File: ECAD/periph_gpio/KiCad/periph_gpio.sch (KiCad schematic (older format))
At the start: 0 parts

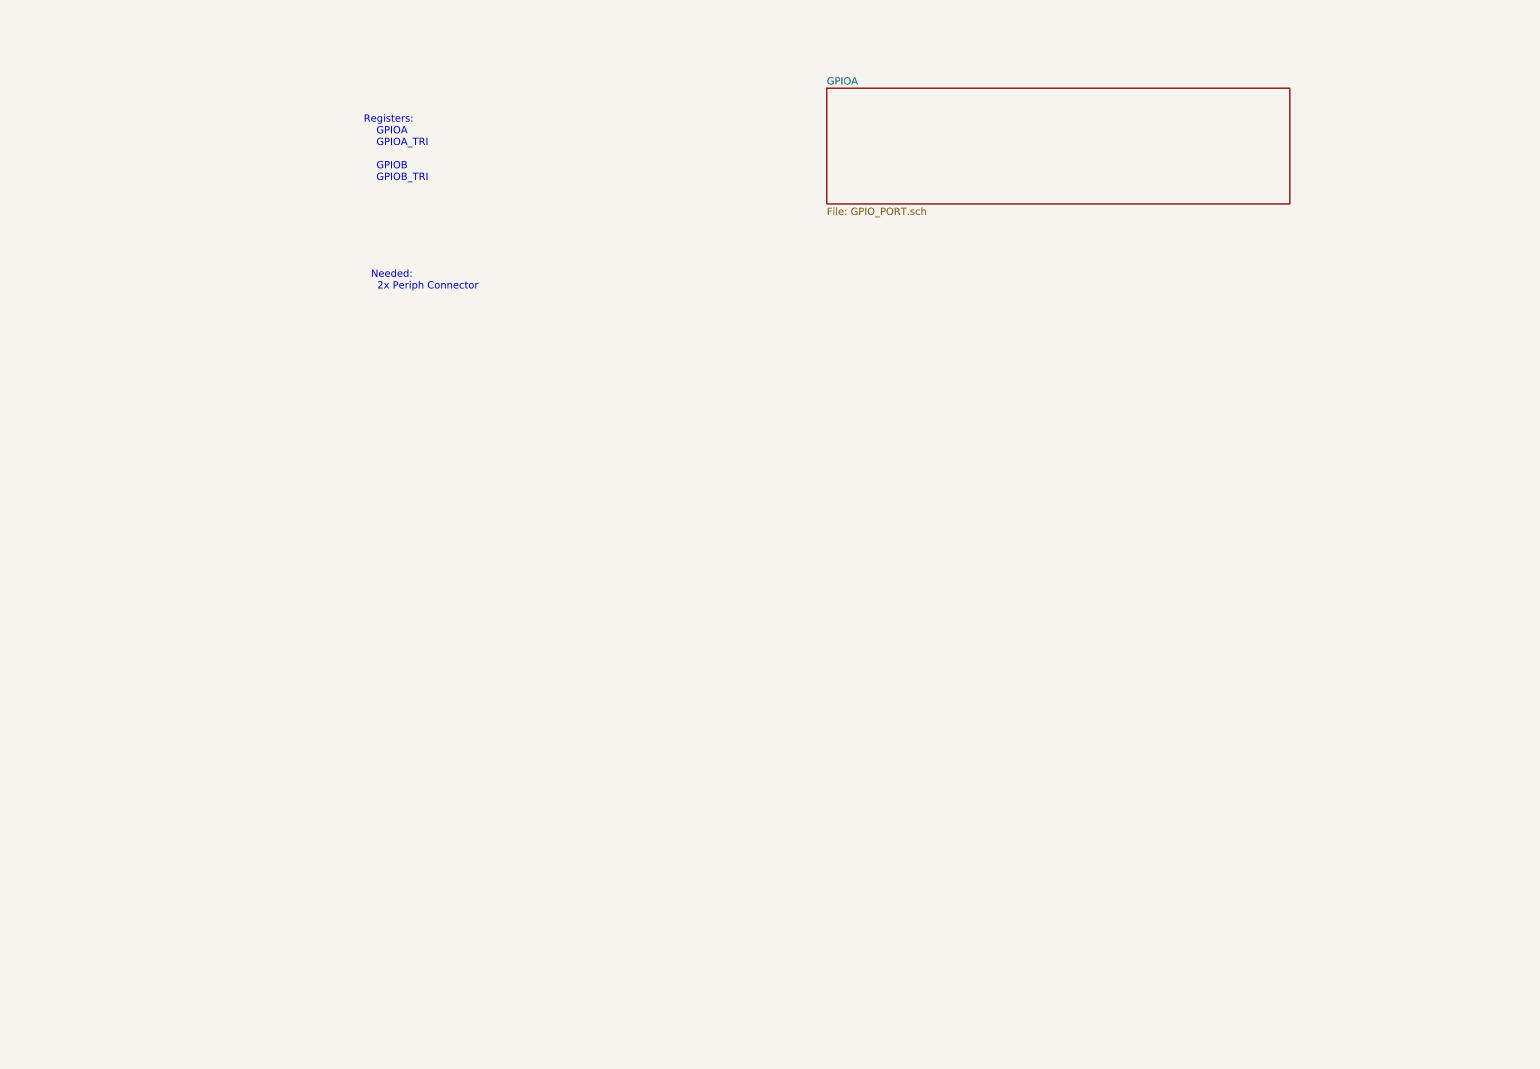
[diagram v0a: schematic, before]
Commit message: First draft v1.0 schematic done, ready for verify
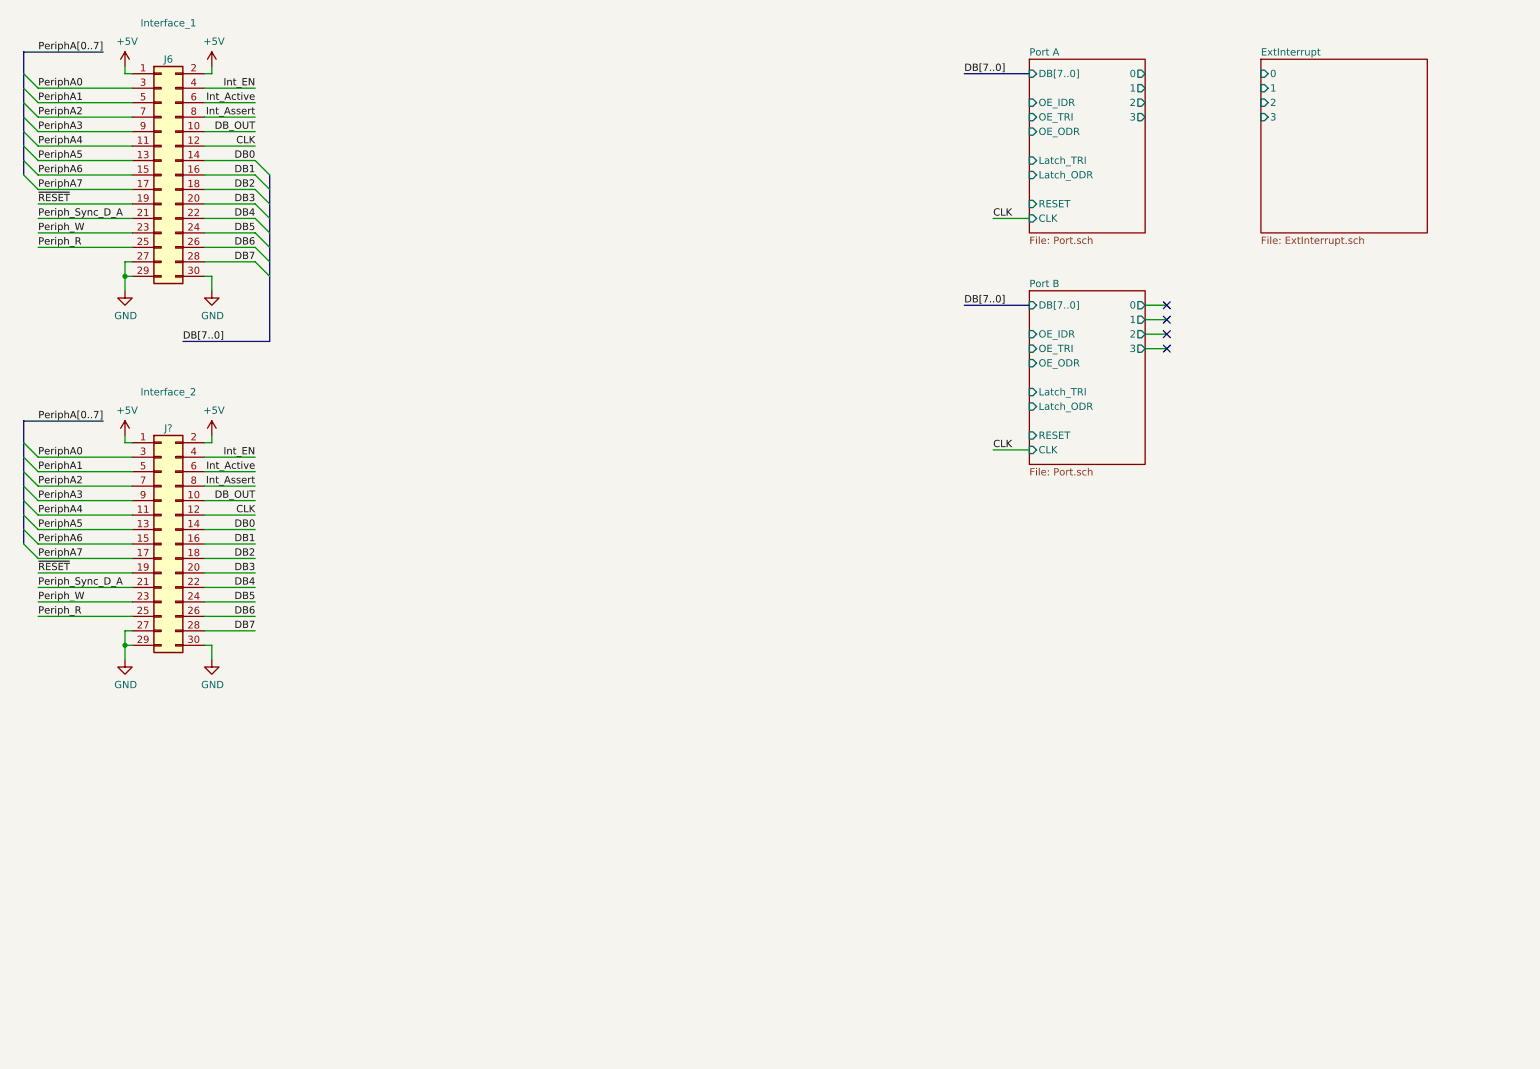
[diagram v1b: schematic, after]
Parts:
- added J6: Interface_1, Connector_IDC:IDC-Header_2x15_P2.54mm_Vertical, symbol Connector_Generic:Conn_02x15_Odd_Even
- added J?: Interface_2, Connector_IDC:IDC-Header_2x15_P2.54mm_Vertical, symbol Connector_Generic:Conn_02x15_Odd_Even
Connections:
- new net +5V: J6.1 (Pin_1), J6.2 (Pin_2), J?.1 (Pin_1), J?.2 (Pin_2)
- new net CLK: J6.12 (Pin_12), J?.12 (Pin_12)
- new net DB0: J6.14 (Pin_14), J?.14 (Pin_14)
- new net DB1: J6.16 (Pin_16), J?.16 (Pin_16)
- new net DB2: J6.18 (Pin_18), J?.18 (Pin_18)
- new net DB3: J6.20 (Pin_20), J?.20 (Pin_20)
- new net DB4: J6.22 (Pin_22), J?.22 (Pin_22)
- new net DB5: J6.24 (Pin_24), J?.24 (Pin_24)
- new net DB6: J6.26 (Pin_26), J?.26 (Pin_26)
- new net DB7: J6.28 (Pin_28), J?.28 (Pin_28)
- new net DB_OUT: J6.10 (Pin_10), J?.10 (Pin_10)
- new net GND: J6.27 (Pin_27), J6.29 (Pin_29), J6.30 (Pin_30), J?.27 (Pin_27), J?.29 (Pin_29), J?.30 (Pin_30)
- new net Int_Active: J6.6 (Pin_6), J?.6 (Pin_6)
- new net Int_Assert: J6.8 (Pin_8), J?.8 (Pin_8)
- new net Int_EN: J6.4 (Pin_4), J?.4 (Pin_4)
- new net PeriphA0: J6.3 (Pin_3), J?.3 (Pin_3)
- new net PeriphA1: J6.5 (Pin_5), J?.5 (Pin_5)
- new net PeriphA2: J6.7 (Pin_7), J?.7 (Pin_7)
- new net PeriphA3: J6.9 (Pin_9), J?.9 (Pin_9)
- new net PeriphA4: J6.11 (Pin_11), J?.11 (Pin_11)
- new net PeriphA5: J6.13 (Pin_13), J?.13 (Pin_13)
- new net PeriphA6: J6.15 (Pin_15), J?.15 (Pin_15)
- new net PeriphA7: J6.17 (Pin_17), J?.17 (Pin_17)
- new net Periph_R: J6.25 (Pin_25), J?.25 (Pin_25)
- new net Periph_Sync_D_A: J6.21 (Pin_21), J?.21 (Pin_21)
- new net Periph_W: J6.23 (Pin_23), J?.23 (Pin_23)
- new net ~RESET: J6.19 (Pin_19), J?.19 (Pin_19)
- no-connect marks 0 -> 4
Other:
- note removed: "Needed:\n 2x Periph Connector"
- note removed: "Registers:\n GPIOA\n GPIOA_TRI\n\n GPIOB\n GPIOB_TRI\n"

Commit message: GPIO: Schematic done
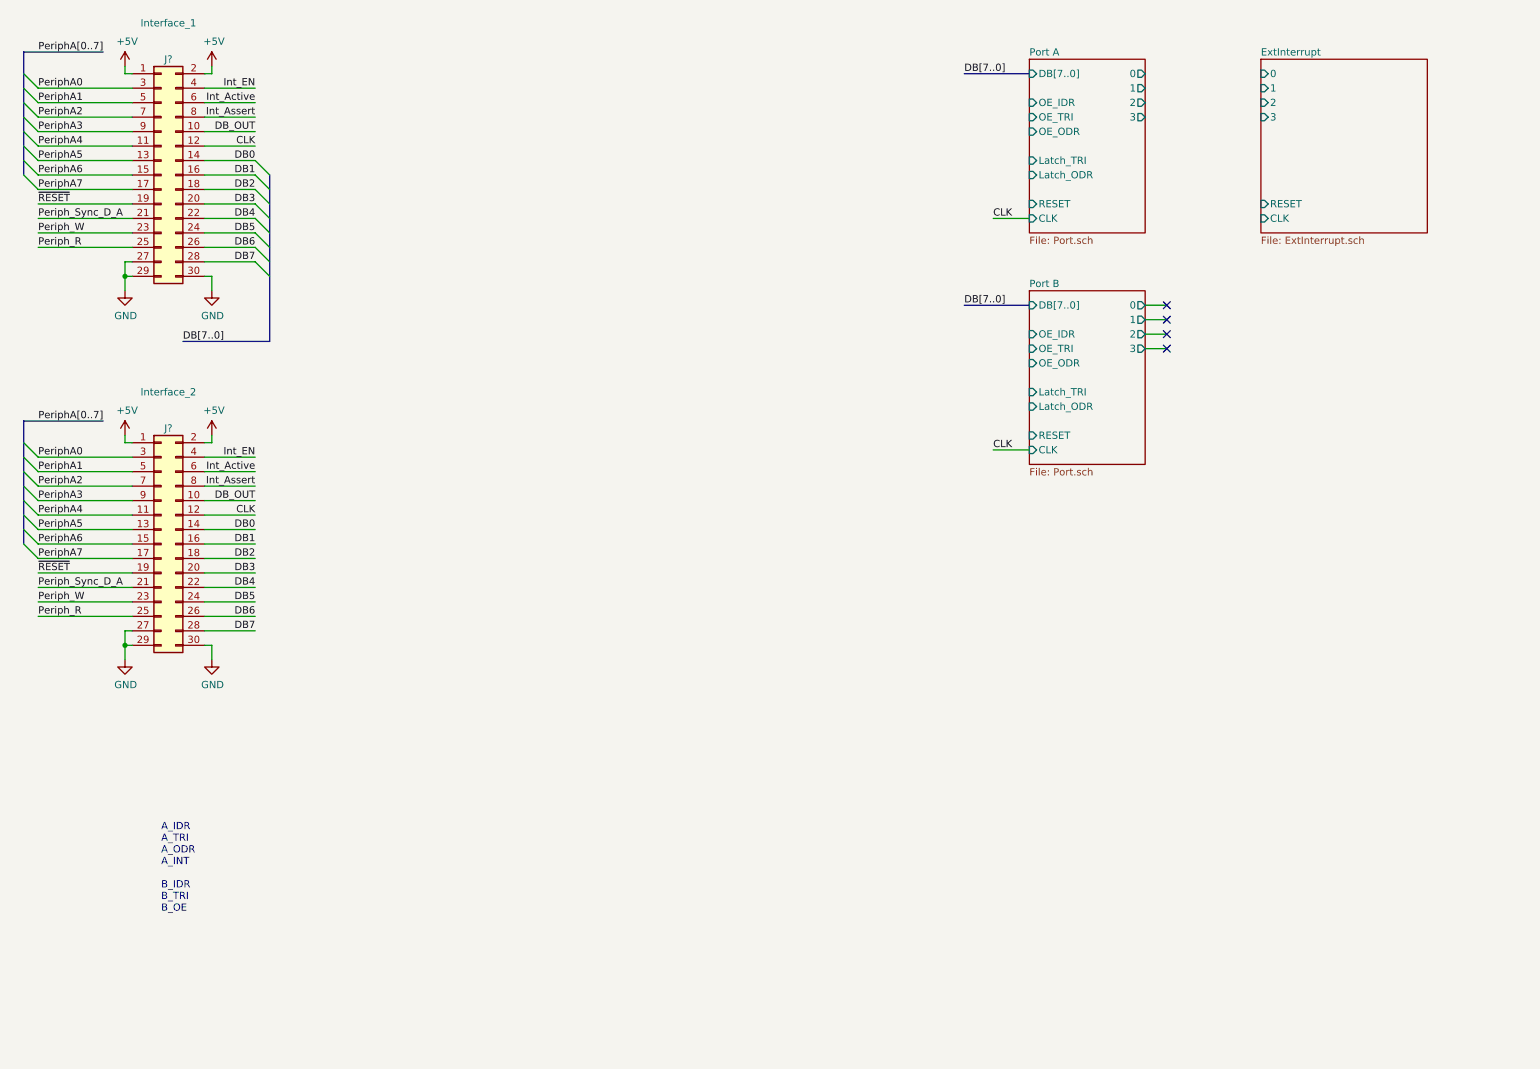
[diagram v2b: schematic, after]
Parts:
- renumbered J6 to J?
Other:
- note added: "A_IDR\nA_TRI\nA_ODR\nA_INT\n\nB_IDR\nB_TRI\nB_OE"
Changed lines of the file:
@@
 $EndSheet
 $Comp
-L Connector_Generic:Conn_02x15_Odd_Even J6
+L Connector_Generic:Conn_02x15_Odd_Even J?
 U 1 1 6012B19C
 P 1550 1650
-F 0 "J6" H 1600 2450 50  0000 C CNN
+F 0 "J?" H 1600 2450 50  0000 C CNN
 F 1 "Interface_1" H 1600 2700 50  0000 C CNN
 F 2 "Connector_IDC:IDC-Header_2x15_P2.54mm_Vertical" H 1550 1650 50  0001 C CNN
@@
 DB7
 $Comp
-L power:+5V #PWR01537
+L power:+5V #PWR?
 U 1 1 601B8799
 P 1300 900
-F 0 "#PWR01537" H 1300 750 50  0001 C CNN
+F 0 "#PWR?" H 1300 750 50  0001 C CNN
 F 1 "+5V" H 1315 1073 50  0000 C CNN
 F 2 "" H 1300 900 50  0001 C CNN
@@
 	1300 950  1350 950
 $Comp
-L power:+5V #PWR01541
+L power:+5V #PWR?
 U 1 1 601BA77E
 P 1900 900
-F 0 "#PWR01541" H 1900 750 50  0001 C CNN
+F 0 "#PWR?" H 1900 750 50  0001 C CNN
 F 1 "+5V" H 1915 1073 50  0000 C CNN
 F 2 "" H 1900 900 50  0001 C CNN
@@
 	1900 2350 1900 2450
 $Comp
-L power:GND #PWR01542
+L power:GND #PWR?
 U 1 1 601E6B8A
 P 1900 2450
-F 0 "#PWR01542" H 1900 2200 50  0001 C CNN
+F 0 "#PWR?" H 1900 2200 50  0001 C CNN
 F 1 "GND" H 1905 2277 50  0000 C CNN
 F 2 "" H 1900 2450 50  0001 C CNN
@@
 $EndComp
 $Comp
-L power:GND #PWR01538
+L power:GND #PWR?
 U 1 1 601E7F01
 P 1300 2450
-F 0 "#PWR01538" H 1300 2200 50  0001 C CNN
+F 0 "#PWR?" H 1300 2200 50  0001 C CNN
 F 1 "GND" H 1305 2277 50  0000 C CNN
 F 2 "" H 1300 2450 50  0001 C CNN
@@
 F4 "2" I L 9150 1150 50
 F5 "3" I L 9150 1250 50
+F6 "RESET" I L 9150 1850 50
+F7 "CLK" I L 9150 1950 50
 $EndSheet
+Text Notes 1550 6750 0    50   ~ 0
+A_IDR\nA_TRI\nA_ODR\nA_INT\n\nB_IDR\nB_TRI\nB_OE
 Wire Bus Line
 	600  800  600  1650

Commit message: GPIO: Layout done / ERC pass
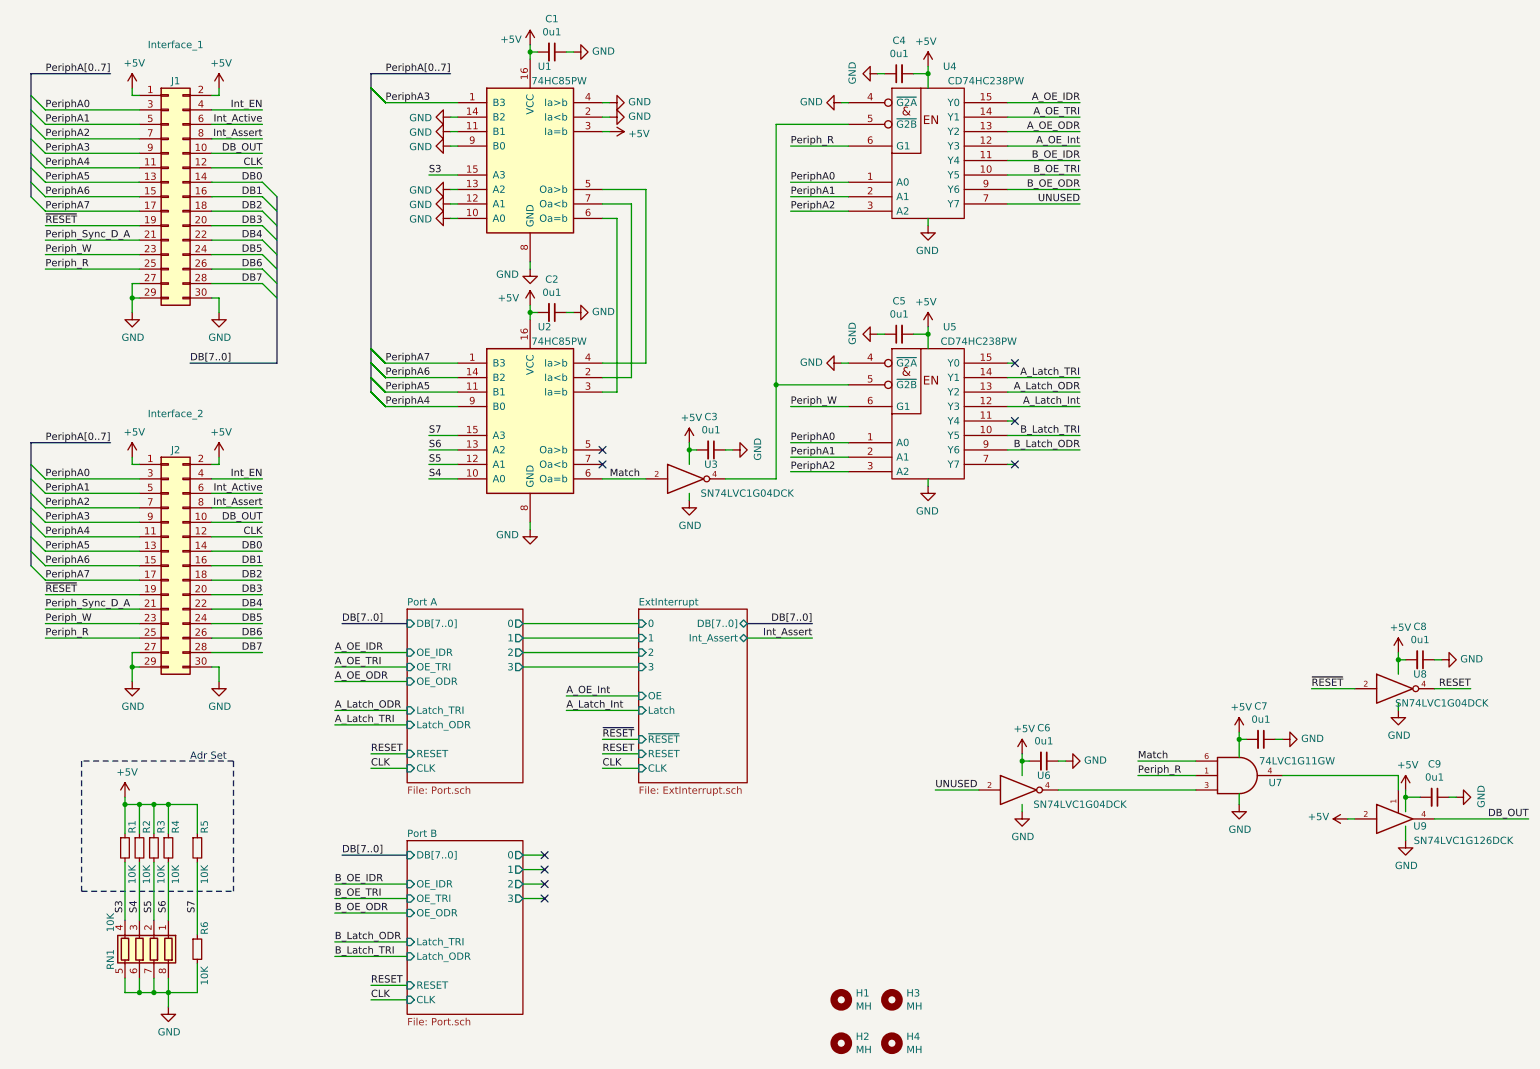
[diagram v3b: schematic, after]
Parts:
- added C1, C2, C3, C4, C5, C6, C7, C8, C9: 0u1, NoRef_Footprints:C_0603_1608Metric_NoRef, symbol Device:C_Small
- added H1, H2, H3, H4: MH, MountingHole:MountingHole_3.2mm_M3_Pad_Via, symbol Mechanical:MountingHole
- added R1, R2, R3, R4, R5, R6: 10K, NoRef_Footprints:R_0603_1608Metric_NoRef, symbol Device:R_Small
- added RN1: 10K, NoRef_Footprints:R_Array_Convex_4x0603_NoRef, symbol Device:R_Pack04
- added U1, U2: 74HC85PW, Package_SO:TSSOP-16_4.4x5mm_P0.65mm, symbol 74xx:74LS85
- added U3, U6, U8: SN74LVC1G04DCK, Package_TO_SOT_SMD:SOT-353_SC-70-5, symbol 74xGxx:74LVC1G04
- added U4, U5: CD74HC238PW, Package_SO:TSSOP-16_4.4x5mm_P0.65mm, symbol 74xx_IEEE:74HC238
- added U7: 74LVC1G11GW, Package_TO_SOT_SMD:SOT-363_SC-70-6, symbol 74xGxx:74LVC1G11
- added U9: SN74LVC1G126DCK, Package_TO_SOT_SMD:SOT-353_SC-70-5, symbol 74xGxx:74LVC1G126
- gave numbers to parts that had none: 2
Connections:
- net +5V: now also C1.2, C2.2, C3.2, C4.2, C5.2, C6.2, C7.2, C8.2, C9.2, R1.1, R2.1, R3.1, R4.1, R5.1, U1.16 (VCC), U1.3 (Ia=b), U2.16 (VCC), U3.5 (VCC), U4.16 (VCC), U5.16 (VCC), U6.5 (VCC), U7.5 (VCC), U8.5 (VCC), U9.2, U9.5 (VCC)
- net DB_OUT: now also U9.4
- net GND: now also C1.1, C2.1, C3.1, C4.1, C5.1, C6.1, C7.1, C8.1, C9.1, R6.2, RN1.5 (R4.2), RN1.6 (R3.2), RN1.7 (R2.2), RN1.8 (R1.2), U1.10 (A0), U1.11 (B1), U1.12 (A1), U1.13 (A2), U1.14 (B2), U1.2 (Ia<b), U1.4 (Ia>b), U1.8 (GND), U1.9 (B0), U2.8 (GND), U3.3 (GND), U4.4 (~G2A), U4.8 (GND), U5.4 (~G2A), U5.8 (GND), U6.3 (GND), U7.2 (GND), U8.3 (GND), U9.3 (GND)
- net PeriphA0: now also U4.1 (A0), U5.1 (A0)
- net PeriphA1: now also U4.2 (A1), U5.2 (A1)
- net PeriphA2: now also U4.3 (A2), U5.3 (A2)
- net PeriphA3: now also U1.1 (B3)
- net PeriphA4: now also U2.9 (B0)
- net PeriphA5: now also U2.11 (B1)
- net PeriphA6: now also U2.14 (B2)
- net PeriphA7: now also U2.1 (B3)
- net Periph_R: now also U4.6 (G1), U7.1
- net Periph_W: now also U5.6 (G1)
- net ~RESET: now also U8.2
- new net: U1.7 (Oa<b), U2.2 (Ia<b)
- new net: U1.6 (Oa=b), U2.3 (Ia=b)
- new net: U1.5 (Oa>b), U2.4 (Ia>b)
- new net: U3.4, U4.5 (~G2B), U5.5 (~G2B)
- new net: U6.4, U7.3
- new net: U7.4, U9.1
- new net A_Latch_Int: U5.12 (Y3)
- new net A_Latch_ODR: U5.13 (Y2)
- new net A_Latch_TRI: U5.14 (Y1)
- new net A_OE_IDR: U4.15 (Y0)
- new net A_OE_Int: U4.12 (Y3)
- new net A_OE_ODR: U4.13 (Y2)
- new net A_OE_TRI: U4.14 (Y1)
- new net B_Latch_ODR: U5.9 (Y6)
- new net B_Latch_TRI: U5.10 (Y5)
- new net B_OE_IDR: U4.11 (Y4)
- new net B_OE_ODR: U4.9 (Y6)
- new net B_OE_TRI: U4.10 (Y5)
- new net Match: U2.6 (Oa=b), U3.2, U7.6
- new net RESET: U8.4
- new net S3: R1.2, RN1.4 (R4.1), U1.15 (A3)
- new net S4: R2.2, RN1.3 (R3.1), U2.10 (A0)
- new net S5: R3.2, RN1.2 (R2.1), U2.12 (A1)
- new net S6: R4.2, RN1.1 (R1.1), U2.13 (A2)
- new net S7: R5.2, R6.1, U2.15 (A3)
- new net UNUSED: U4.7 (Y7), U6.2
- no-connect marks 4 -> 9
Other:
- note added: "Adr Set"
- note removed: "A_IDR\nA_TRI\nA_ODR\nA_INT\n\nB_IDR\nB_TRI\nB_OE"
- moved on the sheet: J1, J2
